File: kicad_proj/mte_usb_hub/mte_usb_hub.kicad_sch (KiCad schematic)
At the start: 21 parts

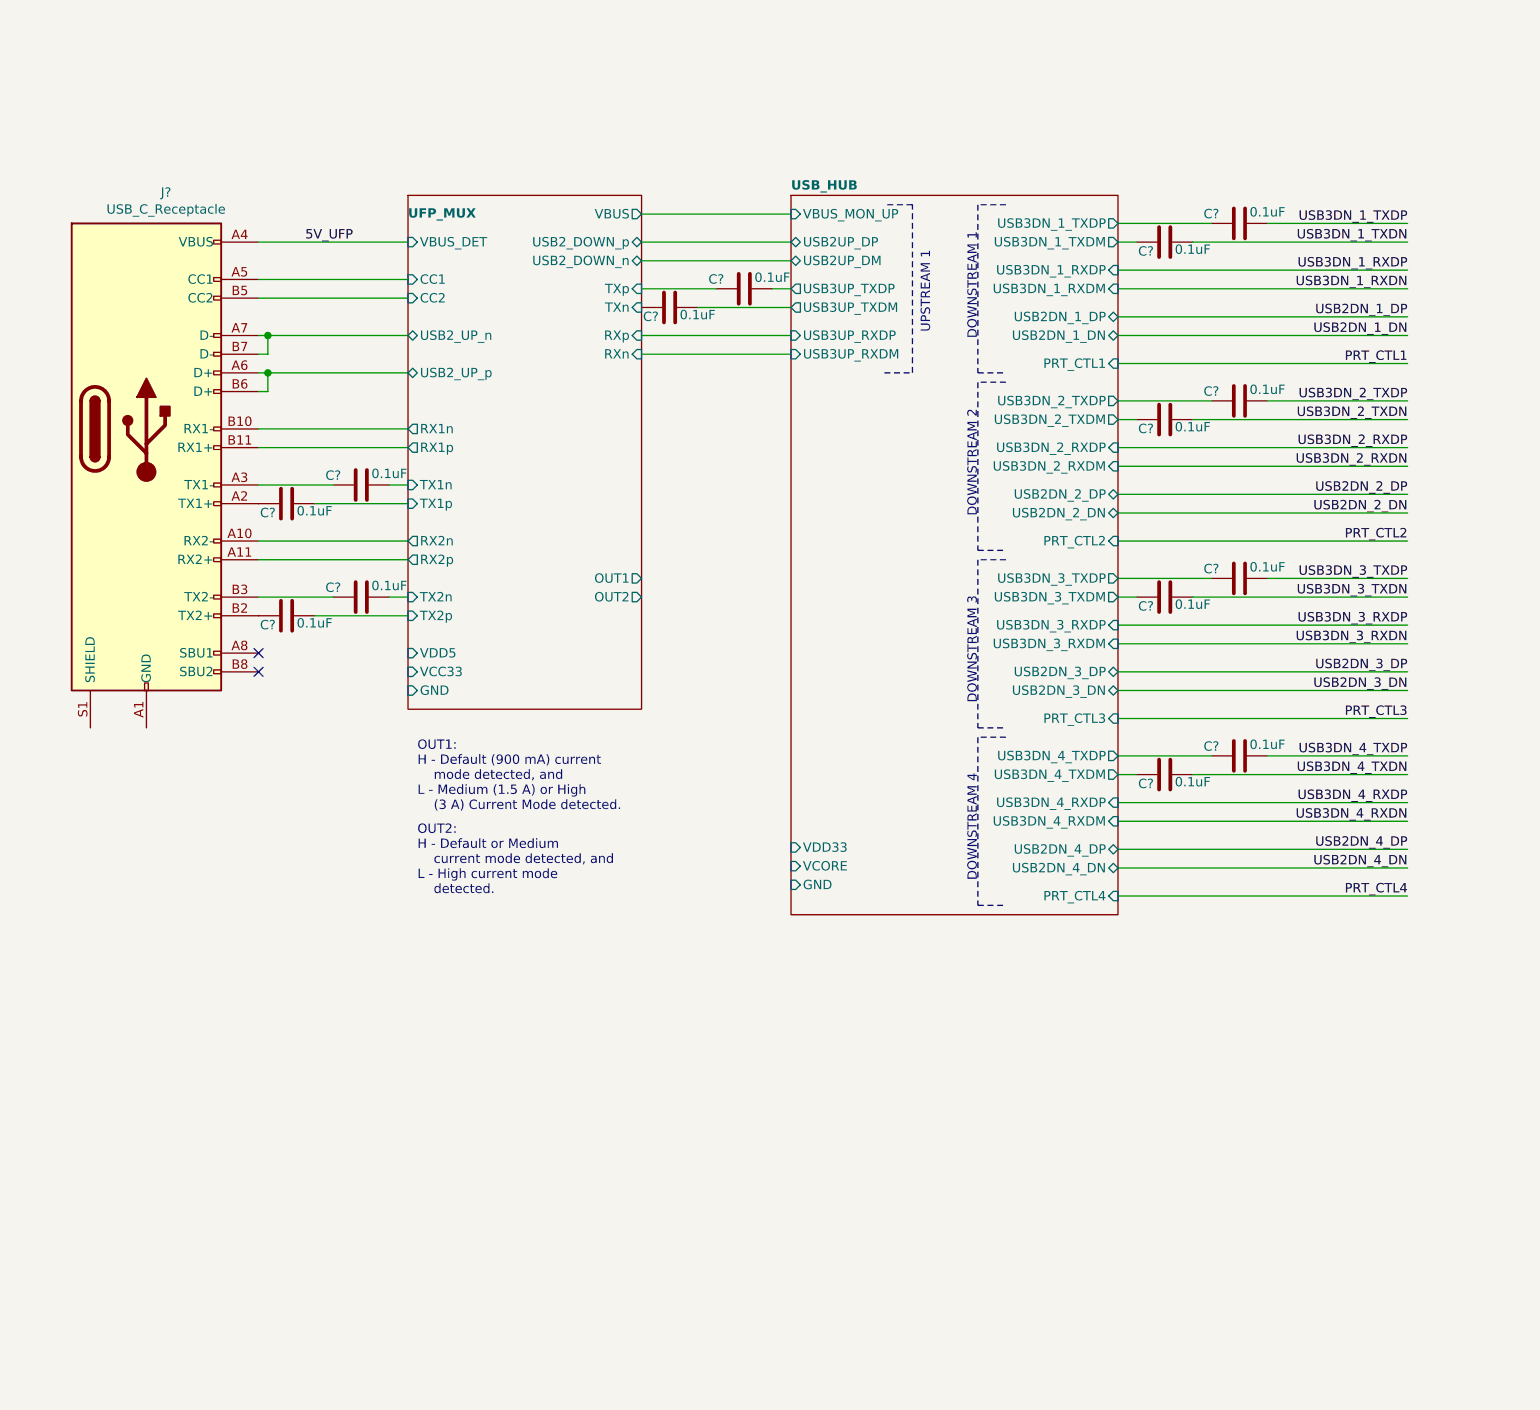
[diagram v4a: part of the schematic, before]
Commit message: Starts power design
Input buck started from 12V -> 5V. One per 2 ports
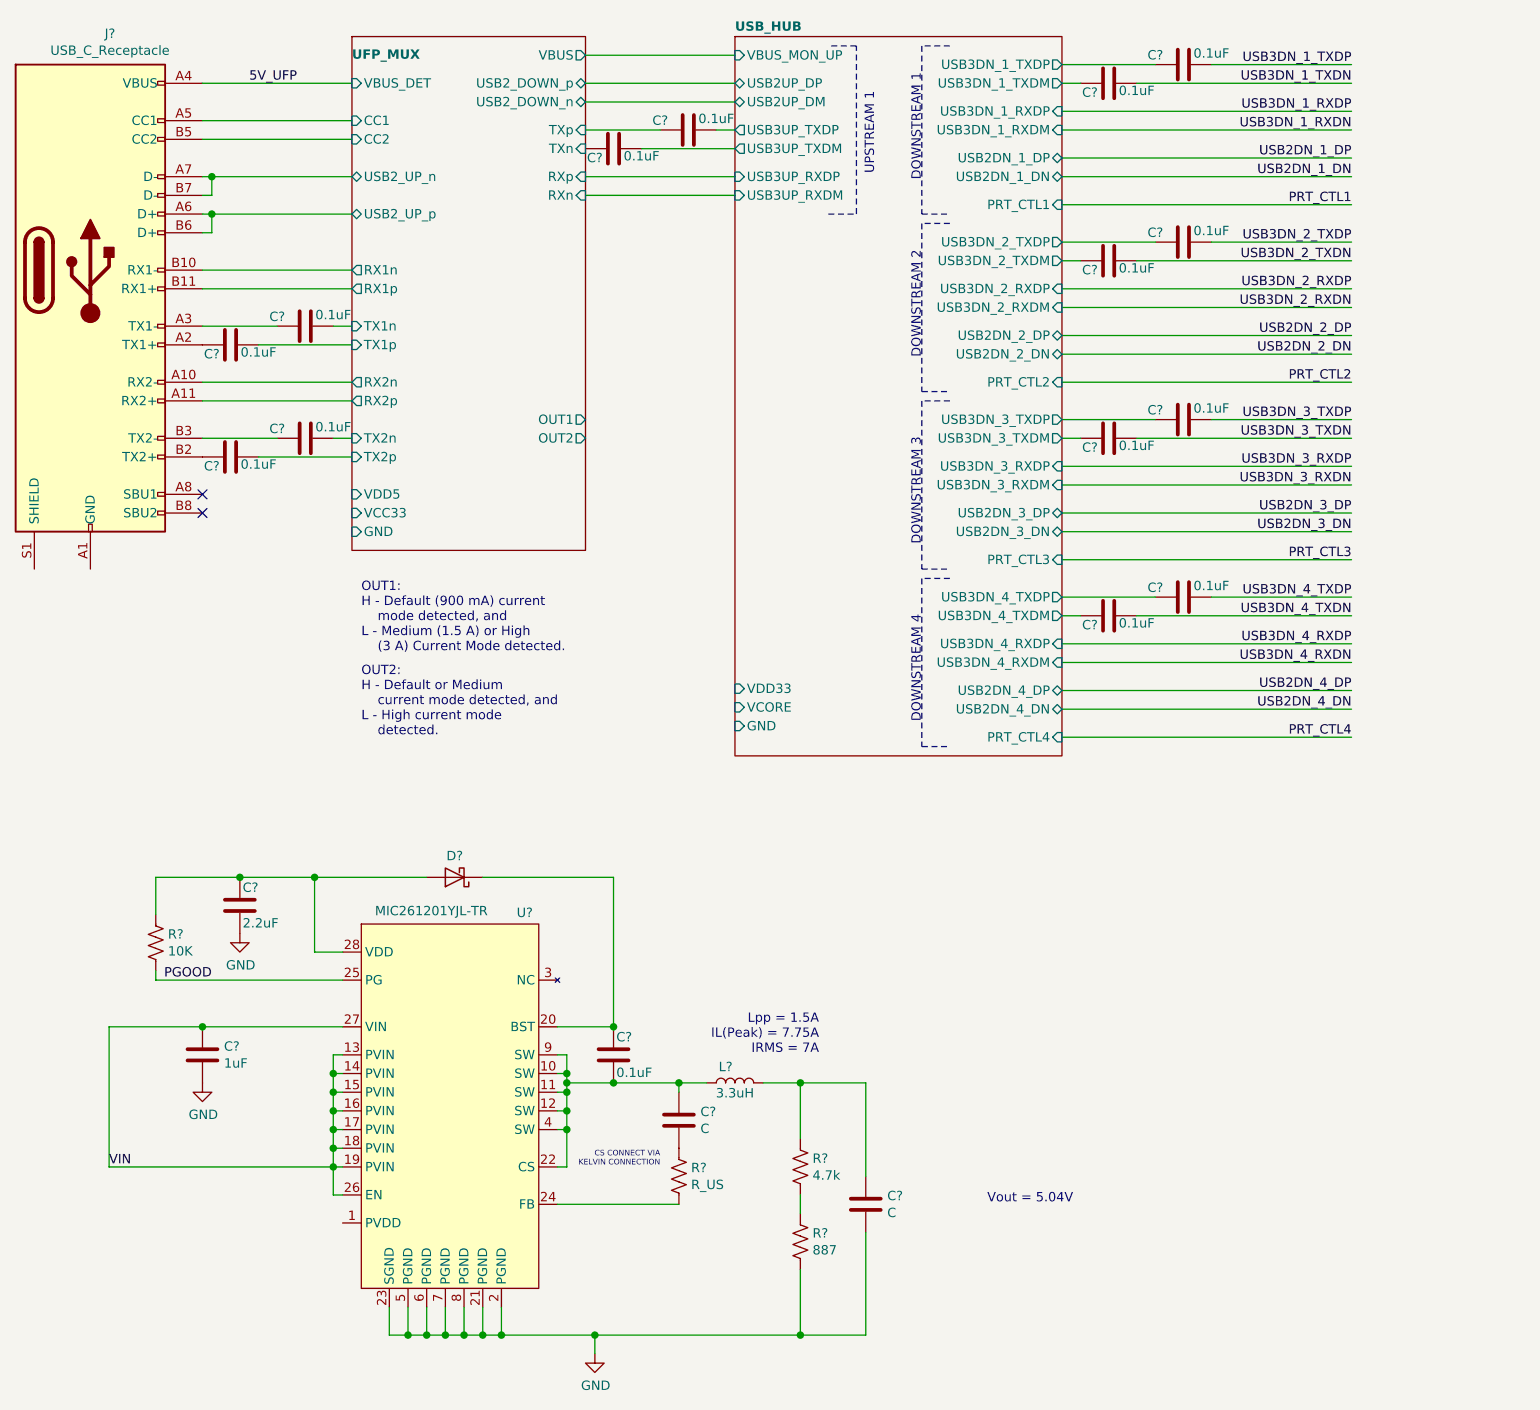
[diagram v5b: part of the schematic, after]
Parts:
- added C?: TMK105CBJ225MV-F, footprints:CAPACITOR_0402N, symbol mte_usb_hub:TMK105CBJ225MV-F
- added C? (x2): C, symbol Device:C
- added C?: CC0402KRX5R7BB104, footprints:CAPACITOR_0402N, symbol mte_usb_hub:CC0402KRX5R7BB104
- added C?: CC0603KRX5R9BB105, footprints:CAPACITOR_0603N, symbol mte_usb_hub:CC0603KRX5R9BB105
- added D?: SS14FL, footprints:DIODE_SMAN, symbol mte_usb_hub:SS14FL
- added L?: PA5007.332NLT, symbol mte_usb_hub:PA5007.332NLT
- added R?: RC0402JR-074K7L, footprints:RESISTOR_0402N, symbol mte_usb_hub:RC0402JR-074K7L
- added R?: RC0402JR-0710KL, footprints:RESISTOR_0402N, symbol mte_usb_hub:RC0402JR-0710KL
- added R?: RC0402FR-07887RL, footprints:RESISTOR_0402N, symbol mte_usb_hub:RC0402FR-07887RL
- added R?: R_US, symbol Device:R_US
- added U?: MIC261201YJL-TR, symbol mte_usb_hub:MIC261201YJL-TR
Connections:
- new net: C?.1, D?.A, R?.1, U?.28 (VDD)
- new net: C?.1, D?.C, U?.20 (BST)
- new net: C?.1, L?.2, R?.1
- new net: R?.1, R?.2
- new net: C?.1, C?.2, L?.1, U?.10 (SW), U?.11 (SW), U?.12 (SW), U?.22 (CS), U?.4 (SW), U?.9 (SW)
- new net: C?.2, R?.1
- new net: R?.2, U?.24 (FB)
- new net GND: C?.2, C?.2, C?.2, R?.2, U?.2 (PGND), U?.21 (PGND), U?.23 (SGND), U?.5 (PGND), U?.6 (PGND), U?.7 (PGND), U?.8 (PGND)
- new net PGOOD: R?.2, U?.25 (PG)
- new net VIN: C?.1, U?.13 (PVIN), U?.14 (PVIN), U?.15 (PVIN), U?.16 (PVIN), U?.17 (PVIN), U?.18 (PVIN), U?.19 (PVIN), U?.26 (EN), U?.27 (VIN)
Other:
- note added: "CS CONNECT VIA KELVIN CONNECTION"
- note added: "Lpp = 1.5A IL(Peak) = 7.75A IRMS = 7A"
- note added: "Vout = 5.04V"
- moved on the sheet: C?, J?

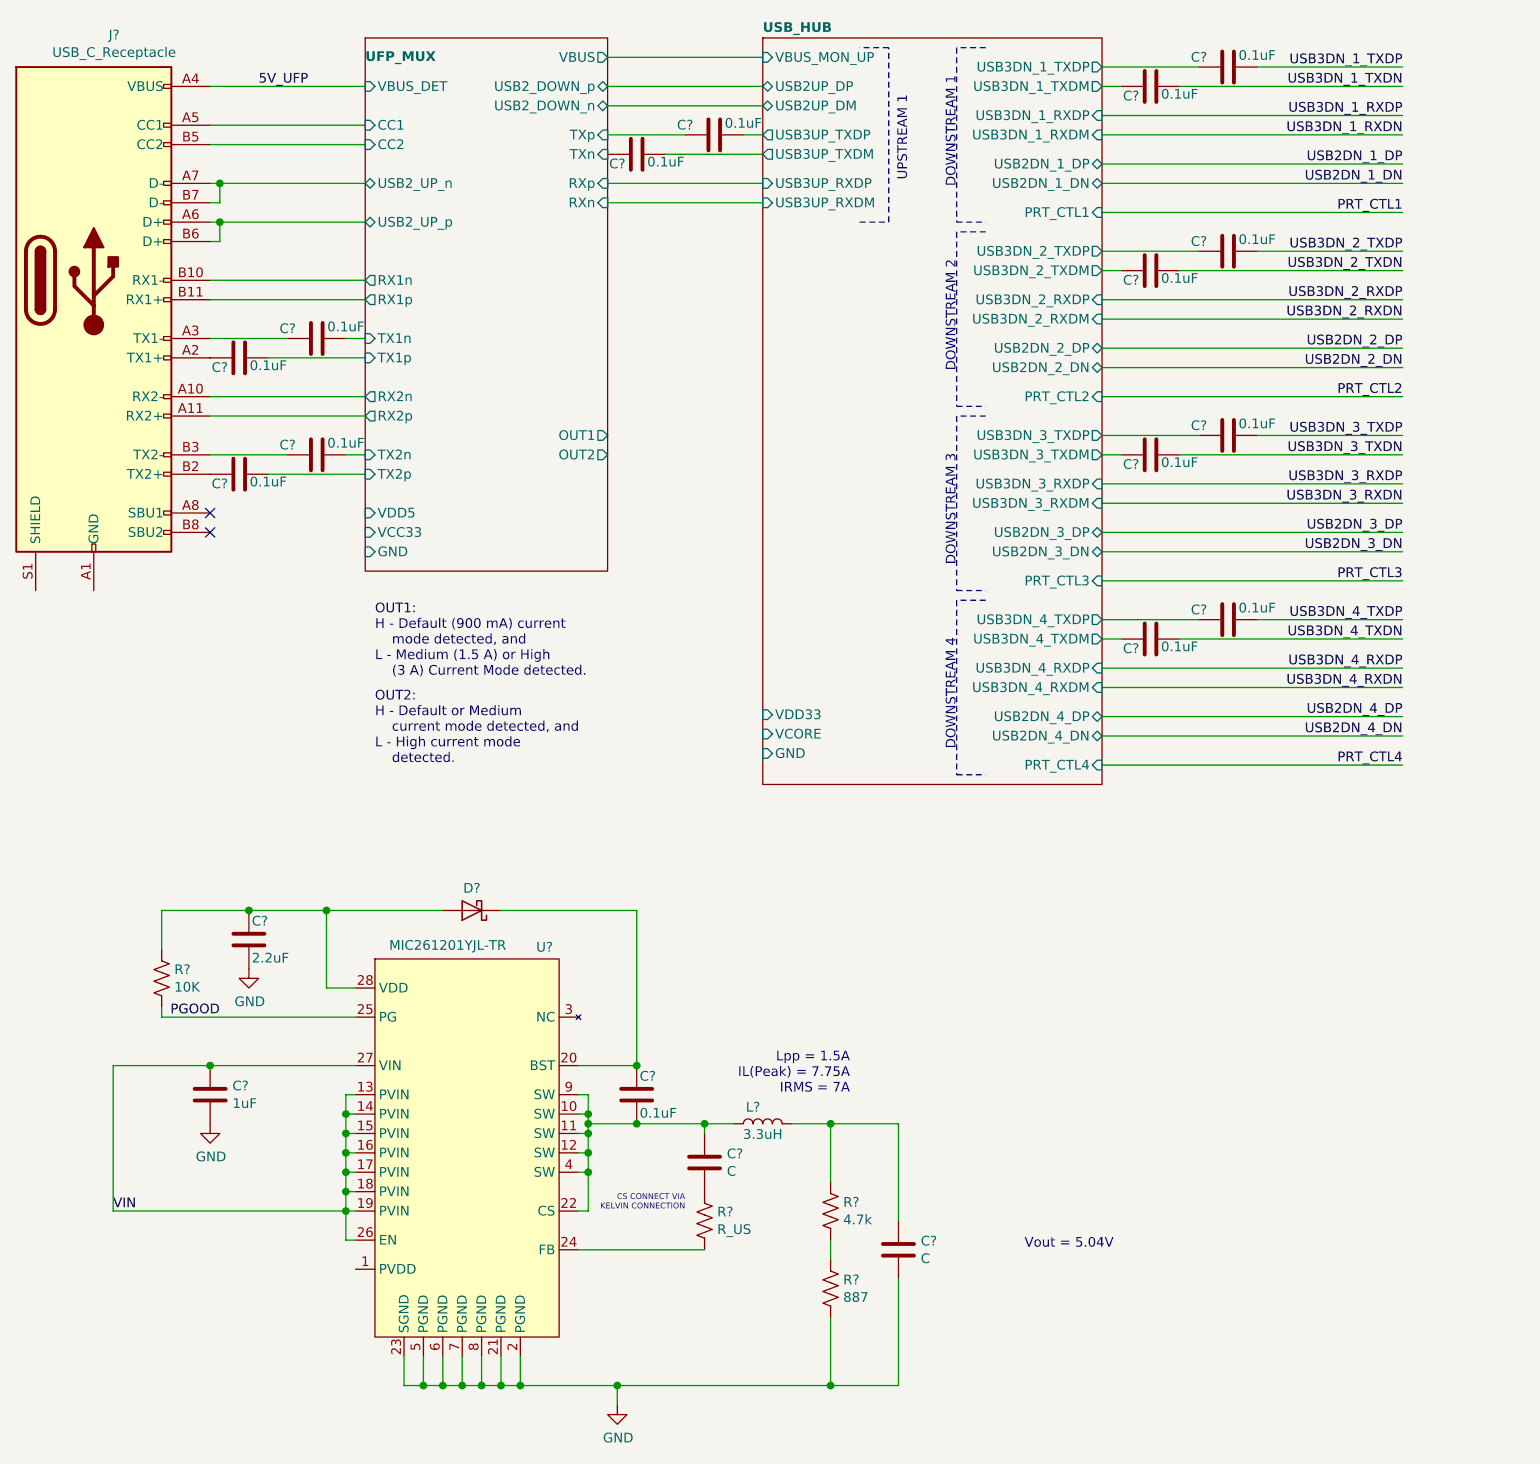
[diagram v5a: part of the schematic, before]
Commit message: Continues power design, replaces Micron Buck with a TI
Micron had a trash datasheet
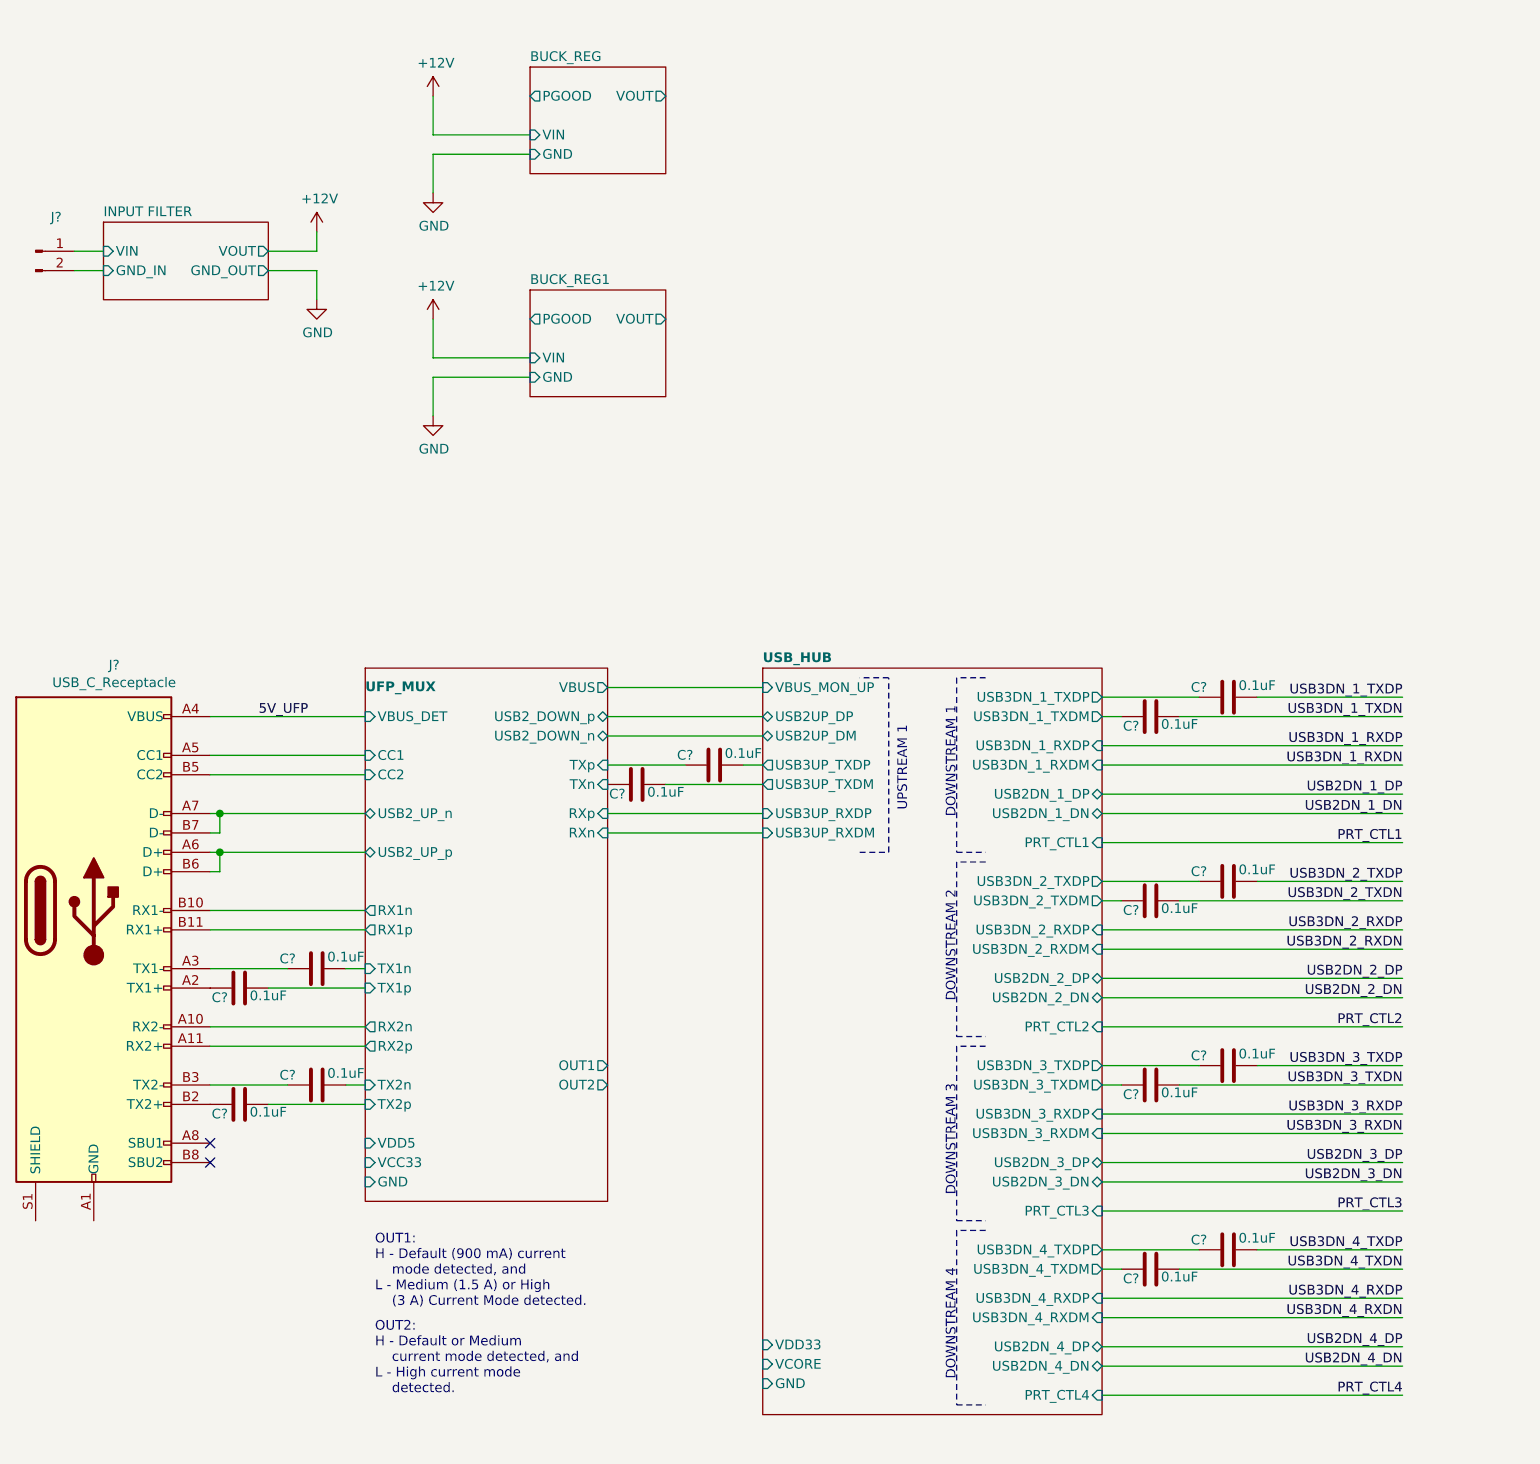
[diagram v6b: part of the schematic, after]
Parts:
- removed C?: TMK105CBJ225MV-F, footprints:CAPACITOR_0402N, symbol mte_usb_hub:TMK105CBJ225MV-F
- removed C? (x2): C, symbol Device:C
- removed C?: CC0402KRX5R7BB104, footprints:CAPACITOR_0402N, symbol mte_usb_hub:CC0402KRX5R7BB104
- removed C?: CC0603KRX5R9BB105, footprints:CAPACITOR_0603N, symbol mte_usb_hub:CC0603KRX5R9BB105
- removed D?: SS14FL, footprints:DIODE_SMAN, symbol mte_usb_hub:SS14FL
- removed L?: PA5007.332NLT, symbol mte_usb_hub:PA5007.332NLT
- removed R?: RC0402JR-074K7L, footprints:RESISTOR_0402N, symbol mte_usb_hub:RC0402JR-074K7L
- removed R?: RC0402JR-0710KL, footprints:RESISTOR_0402N, symbol mte_usb_hub:RC0402JR-0710KL
- removed R?: RC0402FR-07887RL, footprints:RESISTOR_0402N, symbol mte_usb_hub:RC0402FR-07887RL
- removed R?: R_US, symbol Device:R_US
- removed U?: MIC261201YJL-TR, symbol mte_usb_hub:MIC261201YJL-TR
- added J?: Conn_01x02_Male, symbol Connector:Conn_01x02_Male
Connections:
- new net INPUT FILTER/GND_IN: J?.2 (Pin_2)
- new net INPUT FILTER/VIN: J?.1 (Pin_1)
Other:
- added sheet BUCK_REG (buck_reg.kicad_sch)
- added sheet BUCK_REG1 (buck_reg.kicad_sch)
- added sheet INPUT FILTER (input_filter.kicad_sch)
- note removed: "CS CONNECT VIA KELVIN CONNECTION"
- note removed: "Lpp = 1.5A IL(Peak) = 7.75A IRMS = 7A"
- note removed: "Vout = 5.04V"
- moved on the sheet: C?, J?

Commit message: New buck regulator added
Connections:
- net GND: now also J?.10 (SHIELD), J?.10 (SHIELD), J?.10 (SHIELD), J?.10 (SHIELD), J?.4 (GND), J?.4 (GND), J?.4 (GND), J?.4 (GND), J?.7 (DRAIN), J?.7 (DRAIN), J?.7 (DRAIN), J?.7 (DRAIN), J?.A1 (GND), J?.A12 (GND), J?.B1 (GND), J?.B12 (GND), J?.S1 (SHIELD), U?.14 (GND), U?.14 (GND), U?.17 (GND), U?.17 (GND), U?.2 (GND), U?.2 (GND)
- net 5V_2: now reaches U?.10 (VS)
- net 5V_2: now also U?.6 (V_S), U?.7 (V_S), U?.8 (VDD), U?.9 (VS)
- net 5V_1: now reaches U?.10 (VS)
- net 5V_1: now also U?.6 (V_S), U?.7 (V_S), U?.8 (VDD), U?.9 (VS)
- no-connect marks 2 -> 3
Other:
- removed sheet BUCK_REG
- removed sheet BUCK_REG1
- added sheet 5V Buck (5v_buck.kicad_sch)
- note added: "FLOAT TO ENABLE"
- moved on the sheet: J?, U?
